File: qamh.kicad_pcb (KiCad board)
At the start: 2 copper layers, 40.3 x 128.5 mm, 17 parts, among them J1 Eurorack_Power_16pin_Shrouded, J2 OUTPUT, J3 INPUT 1, J4 INPUT 2, J5 INPUT 3

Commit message: fix
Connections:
- A1 pad 21: Net-(A1-Pad21) -> Net-(RV1-Pad2)
- D5 pad 2: Net-(D5-Pad2) -> Net-(RV2-Pad3)
- D6 pad 1: Net-(D5-Pad2) -> Net-(RV2-Pad3)
- J4 pad T: Net-(D5-Pad2) -> Net-(RV2-Pad3)
- RV1 pad 2: Net-(D1-Pad2) -> Net-(RV1-Pad2)
- RV1 pad 3: Net-(A1-Pad21) -> Net-(D1-Pad2)
- RV2 pad 2: Net-(D5-Pad2) -> Net-(A1-Pad20)
- RV2 pad 3: Net-(A1-Pad20) -> Net-(RV2-Pad3)
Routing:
- net Net-(D5-Pad2): track 112.4 -> 0.00 mm
- net Net-(RV2-Pad3): track 0.00 -> 109.2 mm
- net Net-(RV1-Pad2): track 0.00 -> 82.8 mm
- net Net-(A1-Pad21): track 75.3 -> 0.00 mm
- net Net-(A1-Pad19): track 49.7 -> 39.4 mm
- net Net-(A1-Pad20): track 66.6 -> 62.3 mm
- net GND: track 227.3 -> 223.1 mm
- net Net-(A1-Pad22): track 106.7 -> 103.4 mm
- net +5V: track 140.4 -> 138.0 mm
- net Net-(D1-Pad2): track 138.2 -> 138.9 mm

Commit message: fix (2) pot
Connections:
- RV3 pad 2: +5V -> Net-(A1-Pad19)
- RV3 pad 3: Net-(A1-Pad19) -> +5V
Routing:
- net Net-(A1-Pad22): track 103.4 -> 98.9 mm
- net GND: track 223.1 -> 226.2 mm
- net Net-(A1-Pad19): track 39.4 -> 42.3 mm
- net Net-(A1-Pad21): track 82.8 -> 80.3 mm
- net +5V: track 138.0 -> 138.8 mm
- net Net-(A1-Pad20): track 62.3 -> 61.7 mm

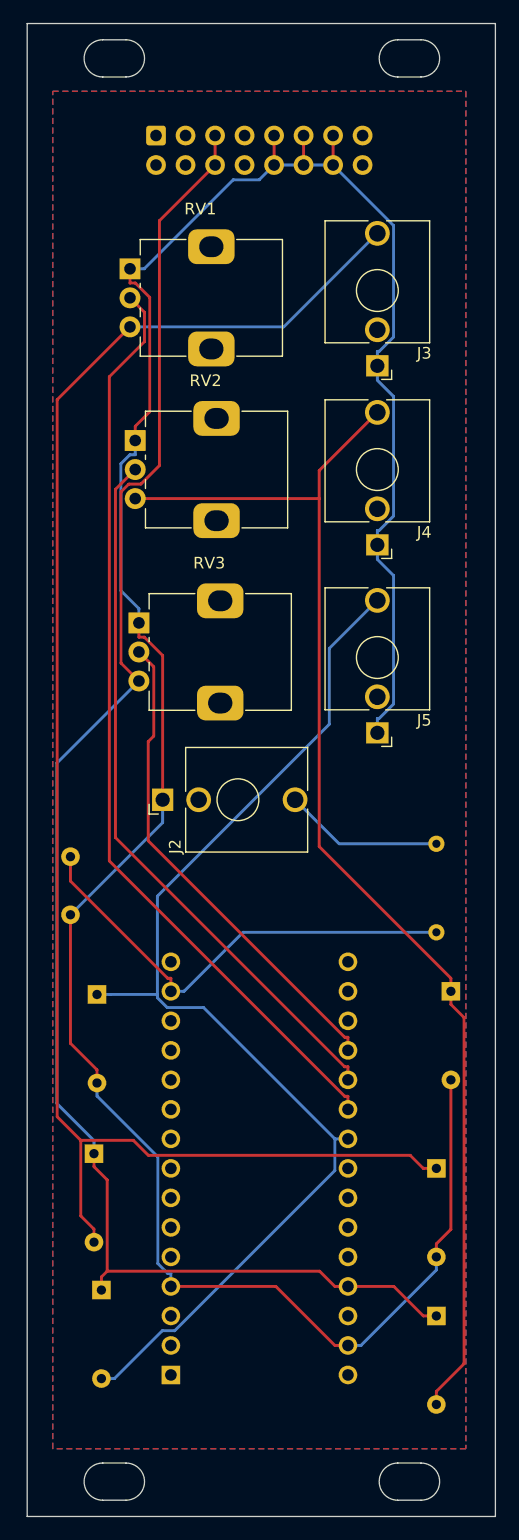
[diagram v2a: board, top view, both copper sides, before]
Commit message: power needs to be fed via the vin of the nano
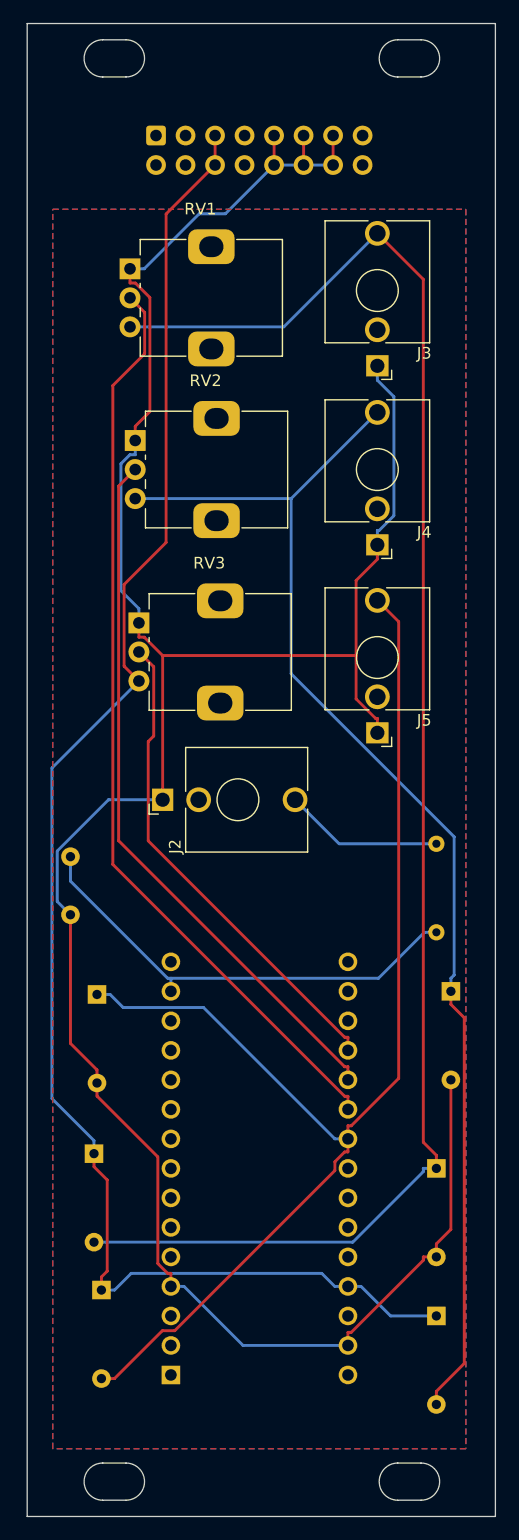
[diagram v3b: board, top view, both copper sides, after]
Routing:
- net Net-(A1-Pad22): track 98.9 -> 106.7 mm
- net GND: track 226.2 -> 226.9 mm
- net Net-(D1-Pad2): track 138.9 -> 139.5 mm
- net +5V: track 138.8 -> 139.4 mm

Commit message: logo's, header for piezo
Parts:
- added G***: LOGO, LOGO, F.Cu at (221.0, 129.5)
- added J6: Conn_01x02_Pin, Connector_PinHeader_2.54mm:PinHeader_1x02_P2.54mm_Vertical, B.Cu at (203.2, 25.4)
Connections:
- A1 pad 27: +5V -> unconnected-(A1-+5V-Pad27)
- A1 pad 30: unconnected-(A1-Pad30) -> +5V
- A1 pad 9: unconnected-(A1-Pad9) -> Net-(A1-D6)
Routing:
- net Net-(A1-D6): track 0.00 -> 89.5 mm
- net Net-(D1-A): track 139.5 -> 156.6 mm
- net GND: track 226.9 -> 238.8 mm
- net Net-(A1-A3): track 106.7 -> 99.1 mm
- net +5V: track 139.4 -> 143.2 mm
- net Net-(A1-A2): track 80.1 -> 79.1 mm
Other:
- board text added: "QAMH, v0.1"
- board text added: "www.vanheusden.com"

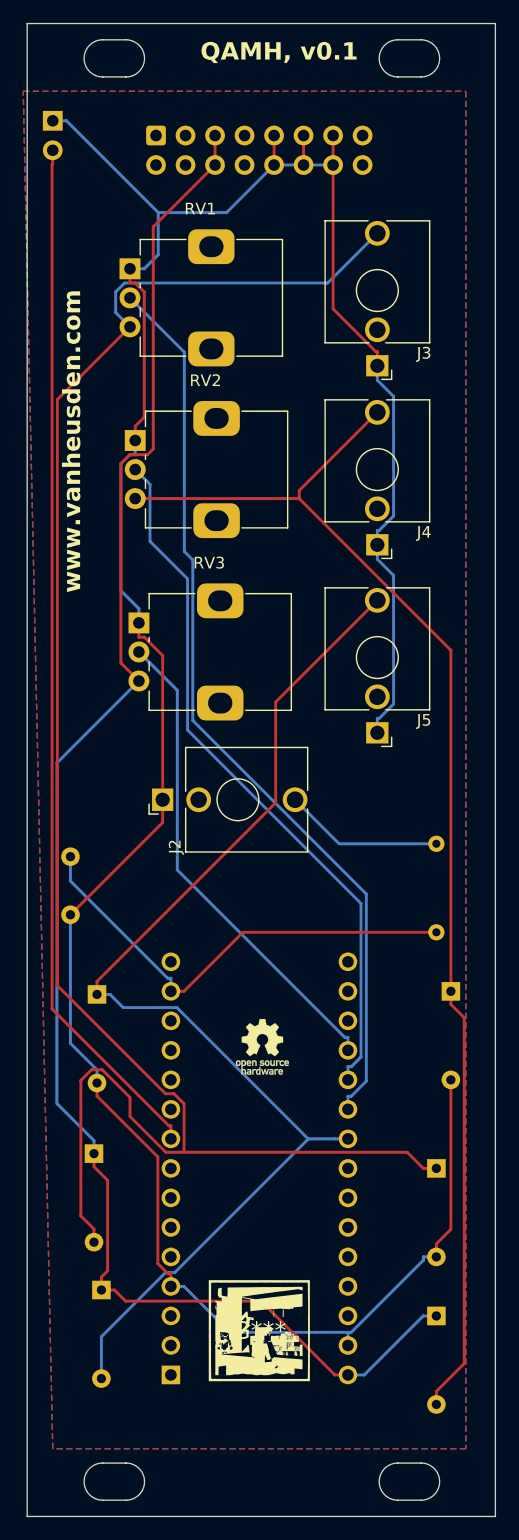
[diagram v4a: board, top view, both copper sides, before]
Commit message: added button to D2
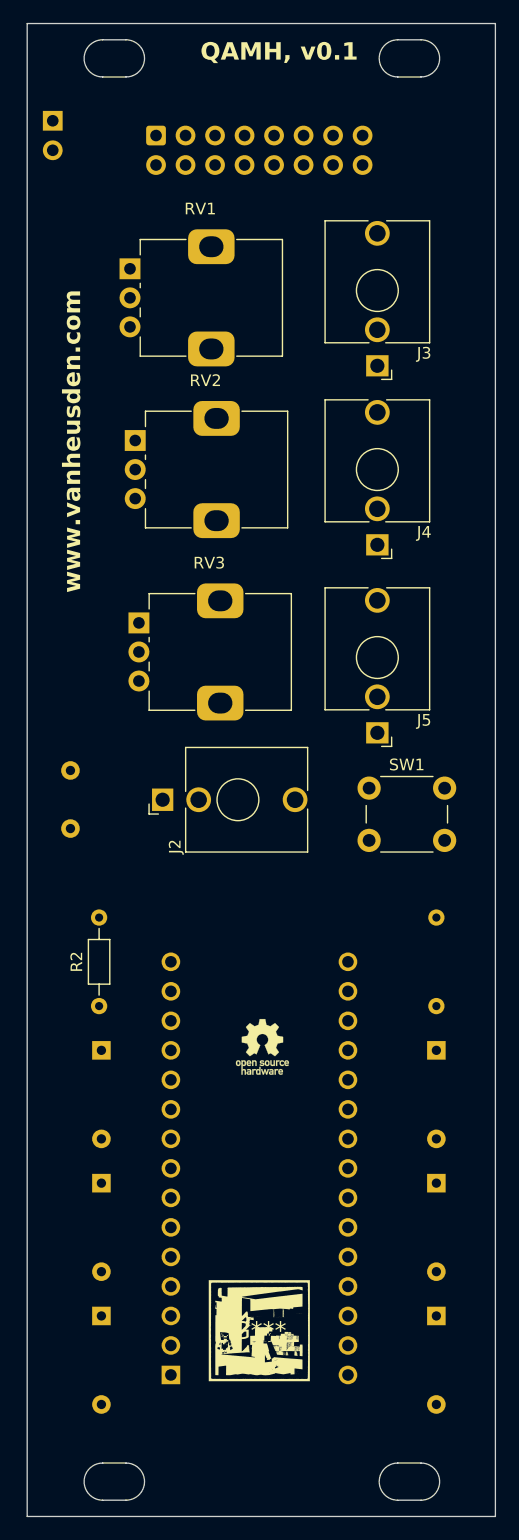
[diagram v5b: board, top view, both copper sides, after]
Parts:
- added R2: 10k, Resistor_THT:R_Axial_DIN0204_L3.6mm_D1.6mm_P7.62mm_Horizontal, F.Cu at (207.2, 101.6)
- added SW1: SW_Push, Button_Switch_THT:SW_PUSH_6mm_H5mm, F.Cu at (230.4, 82.8)
- RV1: value P1 -> B10K (linear 10k ohm)
- RV2: value P2 -> B10K
- RV3: value P3 -> B10K
- moved C1 7.42 mm to (204.7, 81.3)
- moved R1 6.35 mm to (236.2, 94.0)
- moved D6 5.23 mm to (236.2, 105.4)
- moved D4 4.82 mm to (207.4, 105.4)
- moved D1 2.62 mm to (207.4, 116.8)
- moved D3 2.23 mm to (207.4, 128.3)
- moved D2 1.27 mm to (236.2, 116.8)
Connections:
- A1 pad 5: unconnected-(A1-D2-Pad5) -> Net-(A1-D2)
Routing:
- net GND: track 238.8 -> 0.00 mm
- net Net-(D1-A): track 156.6 -> 0.00 mm
- net +5V: track 143.2 -> 0.00 mm
- net Net-(D5-A): track 109.2 -> 0.00 mm
- net Net-(A1-A3): track 99.1 -> 0.00 mm
- net Net-(A1-D6): track 89.5 -> 0.00 mm
- net Net-(A1-A2): track 79.1 -> 0.00 mm
- net Net-(A1-A1): track 61.2 -> 0.00 mm
- net Net-(A1-A0): track 41.9 -> 0.00 mm
- net Net-(A1-MOSI): track 40.3 -> 0.00 mm
- net Net-(J2-PadT): track 13.7 -> 0.00 mm
- removed copper zone on B.Cu, net GND
- removed copper zone on F.Cu, net GND

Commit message: header for plug/unplug 5V
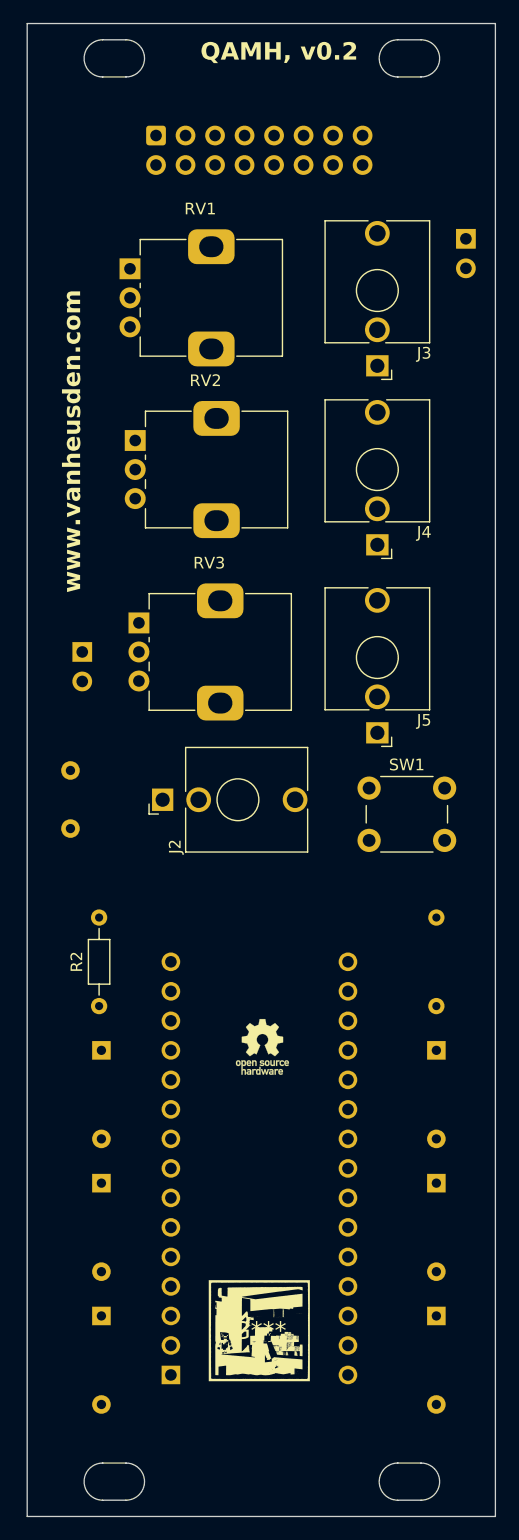
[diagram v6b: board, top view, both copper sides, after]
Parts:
- added J7: Conn_01x02, Connector_PinHeader_2.54mm:PinHeader_1x02_P2.54mm_Vertical, B.Cu at (238.8, 35.6)
- moved J6 45.8 mm to (205.7, 71.1)
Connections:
- A1 pad 30: +5V -> Net-(A1-VIN)
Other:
- board text added: "QAMH, v0.2"
- board text removed: "QAMH, v0.1"
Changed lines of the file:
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@@
   (net 39 "unconnected-(J1-P16-Pad16)")
   (net 40 "Net-(J2-PadT)")
+  (net 41 "Net-(A1-VIN)")
   (footprint "Connector_Audio:Jack_3.5mm_QingPu_WQP-PJ398SM_Vertical_CircularHoles" (layer "F.Cu")
     (at 231.14 46.49 180)
@@
     )
   )
+  (footprint "Connector_PinHeader_2.54mm:PinHeader_1x02_P2.54mm_Vertical" (layer "B.Cu")
+    (at 238.76 35.56 180)
+    (descr "Through hole straight pin header, 1x02, 2.54mm pitch, single row")
+    (tags "Through hole pin header THT 1x02 2.54mm single row")
+    (property "Manufacturer" "TAD")
+    (property "Part Number" "1-0201FBV0T")
+    (property "Production Stage" "B")
+    (property "Sheetfile" "qamh.kicad_sch")
+    (property "Sheetname" "")
+    (property "Specifications" "Pins_01x02, Header, Male Pins, 1*2, spacing 2.54mm, straight pin")
+    (property "ki_description" "HEADER 1x2 MALE PINS 0.100” 180deg")
+    (property "ki_keywords" "Conn_01x02")
+    (attr through_hole)
+    (fp_text reference "J7" (at 0 2.33) (layer "B.SilkS")
+        (effects (font (size 1 1) (thickness 0.15)) (justify mirror))
+    )
+    (fp_text value "Conn_01x02" (at 0 -4.87) (layer "B.Fab")
+        (effects (font (size 1 1) (thickness 0.15)) (justify mirror))
+    )
+    (fp_text user "${REFERENCE}" (at 0 -1.27 90) (layer "B.Fab")
+        (effects (font (size 1 1) (thickness 0.15)) (justify mirror))
+    )
+    (fp_line (start -1.33 -3.87) (end 1.33 -3.87)
+      (stroke (width 0.12) (type solid)) (layer "B.SilkS"))
+    (fp_line (start -1.33 -1.27) (end -1.33 -3.87)
+      (stroke (width 0.12) (type solid)) (layer "B.SilkS"))
+    (fp_line (start -1.33 -1.27) (end 1.33 -1.27)
+      (stroke (width 0.12) (type solid)) (layer "B.SilkS"))
+    (fp_line (start -1.33 0) (end -1.33 1.33)
+      (stroke (width 0.12) (type solid)) (layer "B.SilkS"))
+    (fp_line (start -1.33 1.33) (end 0 1.33)
+      (stroke (width 0.12) (type solid)) (layer "B.SilkS"))
+    (fp_line (start 1.33 -1.27) (end 1.33 -3.87)
+      (stroke (width 0.12) (type solid)) (layer "B.SilkS"))
+    (fp_line (start -1.8 -4.35) (end 1.8 -4.35)
+      (stroke (width 0.05) (type solid)) (layer "B.CrtYd"))
+    (fp_line (start -1.8 1.8) (end -1.8 -4.35)
+      (stroke (width 0.05) (type solid)) (layer "B.CrtYd"))
+    (fp_line (start 1.8 -4.35) (end 1.8 1.8)
+      (stroke (width 0.05) (type solid)) (layer "B.CrtYd"))
+    (fp_line (start 1.8 1.8) (end -1.8 1.8)
+      (stroke (width 0.05) (type solid)) (layer "B.CrtYd"))
+    (fp_line (start -1.27 -3.81) (end -1.27 0.635)
+      (stroke (width 0.1) (type solid)) (layer "B.Fab"))
+    (fp_line (start -1.27 0.635) (end -0.635 1.27)
+      (stroke (width 0.1) (type solid)) (layer "B.Fab"))
+    (fp_line (start -0.635 1.27) (end 1.27 1.27)
+      (stroke (width 0.1) (type solid)) (layer "B.Fab"))
+    (fp_line (start 1.27 -3.81) (end -1.27 -3.81)
+      (stroke (width 0.1) (type solid)) (layer "B.Fab"))
+    (fp_line (start 1.27 1.27) (end 1.27 -3.81)
+      (stroke (width 0.1) (type solid)) (layer "B.Fab"))
+    (pad "1" thru_hole rect (at 0 0 180) (size 1.7 1.7) (drill 1) (layers "*.Cu" "*.Mask")
+      (net 27 "+5V") (pinfunction "Pin_1") (pintype "passive"))
+    (pad "2" thru_hole oval (at 0 -2.54 180) (size 1.7 1.7) (drill 1) (layers "*.Cu" "*.Mask")
+      (net 41 "Net-(A1-VIN)") (pinfunction "Pin_2") (pintype "passive"))
+    (model "${KICAD6_3DMODEL_DIR}/Connector_PinHeader_2.54mm.3dshapes/PinHeader_1x02_P2.54mm_Vertical.wrl"
+      (offset (xyz 0 0 0))
+      (scale (xyz 1 1 1))
+      (rotate (xyz 0 0 0))
+    )
+  )
   (footprint "Diode_THT:D_DO-35_SOD27_P7.62mm_Horizontal" (layer "B.Cu")
     (at 236.22 128.27 -90)
@@
       (net 4 "GND") (pinfunction "GND") (pintype "passive"))
     (pad "30" thru_hole oval (at 15.24 0) (size 1.6 1.6) (drill 1) (layers "*.Cu" "*.Mask")
-      (net 27 "+5V") (pinfunction "VIN") (pintype "power_in"))
+      (net 41 "Net-(A1-VIN)") (pinfunction "VIN") (pintype "power_in"))
     (model "${KICAD6_3DMODEL_DIR}/Module.3dshapes/Arduino_Nano_WithMountingHoles.wrl"
       (offset (xyz 0 0 0))
@@
   )
   (footprint "Connector_PinHeader_2.54mm:PinHeader_1x02_P2.54mm_Vertical" (layer "B.Cu")
-    (at 203.2 25.4 180)
+    (at 205.74 71.12 180)
     (descr "Through hole straight pin header, 1x02, 2.54mm pitch, single row")
     (tags "Through hole pin header THT 1x02 2.54mm single row")
@@
   (gr_line (start 209.5 140.93) (end 207.5 140.93)
     (stroke (width 0.05) (type solid)) (layer "Edge.Cuts"))
-  (gr_text "QAMH, v0.1" (at 215.9 20.32) (layer "F.SilkS")
+  (gr_text "QAMH, v0.2" (at 215.9 20.32) (layer "F.SilkS")
     (effects (font (size 1.5 1.5) (thickness 0.3) bold) (justify left bottom))
   )
